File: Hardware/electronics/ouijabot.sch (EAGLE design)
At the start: 12 parts, among them J1 RASPBERRYPI-40-PIN-GPIO_PTH_N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

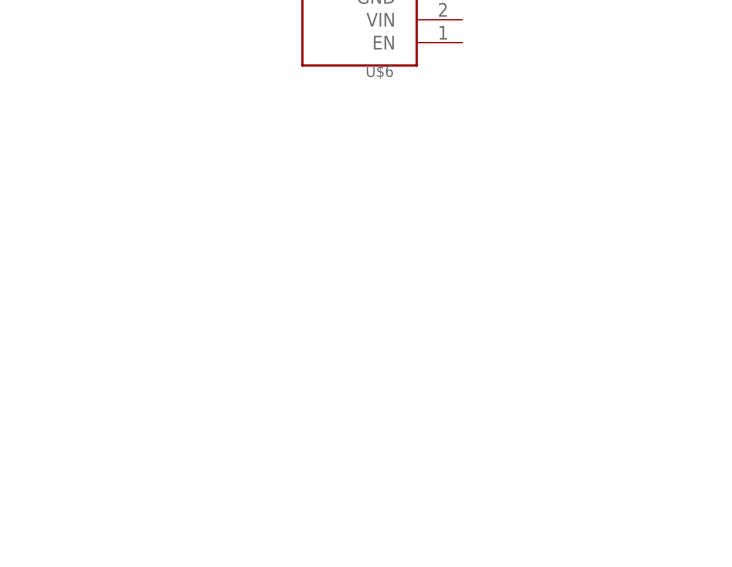
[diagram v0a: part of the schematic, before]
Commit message: Added USB header to schematic.
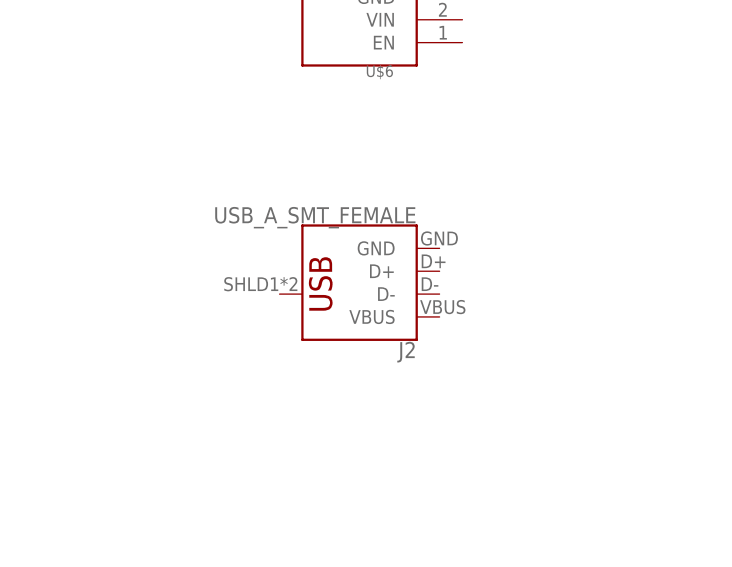
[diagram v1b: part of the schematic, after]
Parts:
- added J2: USB_A_SMT_FEMALE, SparkFun-Connectors:USB_A_SMT_FEMALE
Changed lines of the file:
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@@
 <part name="U$8" library="ouijabot" deviceset="TB9051FTG" device=""/>
 <part name="U$9" library="ouijabot" deviceset="TB9051FTG" device=""/>
+<part name="J2" library="SparkFun-Connectors" deviceset="USB_A" device="_SMT_FEMALE"/>
 </parts>
 <sheets>
@@
 <attribute name="VALUE" x="213.36" y="25.4" size="1.27" layer="96"/>
 </instance>
+<instance part="J2" gate="G$1" x="45.72" y="119.38" smashed="yes" rot="R180">
+<attribute name="NAME" x="50.8" y="111.506" size="1.778" layer="95" font="vector" rot="R180"/>
+<attribute name="VALUE" x="50.8" y="124.714" size="1.778" layer="96" font="vector" rot="R180" align="top-left"/>
+</instance>
 </instances>

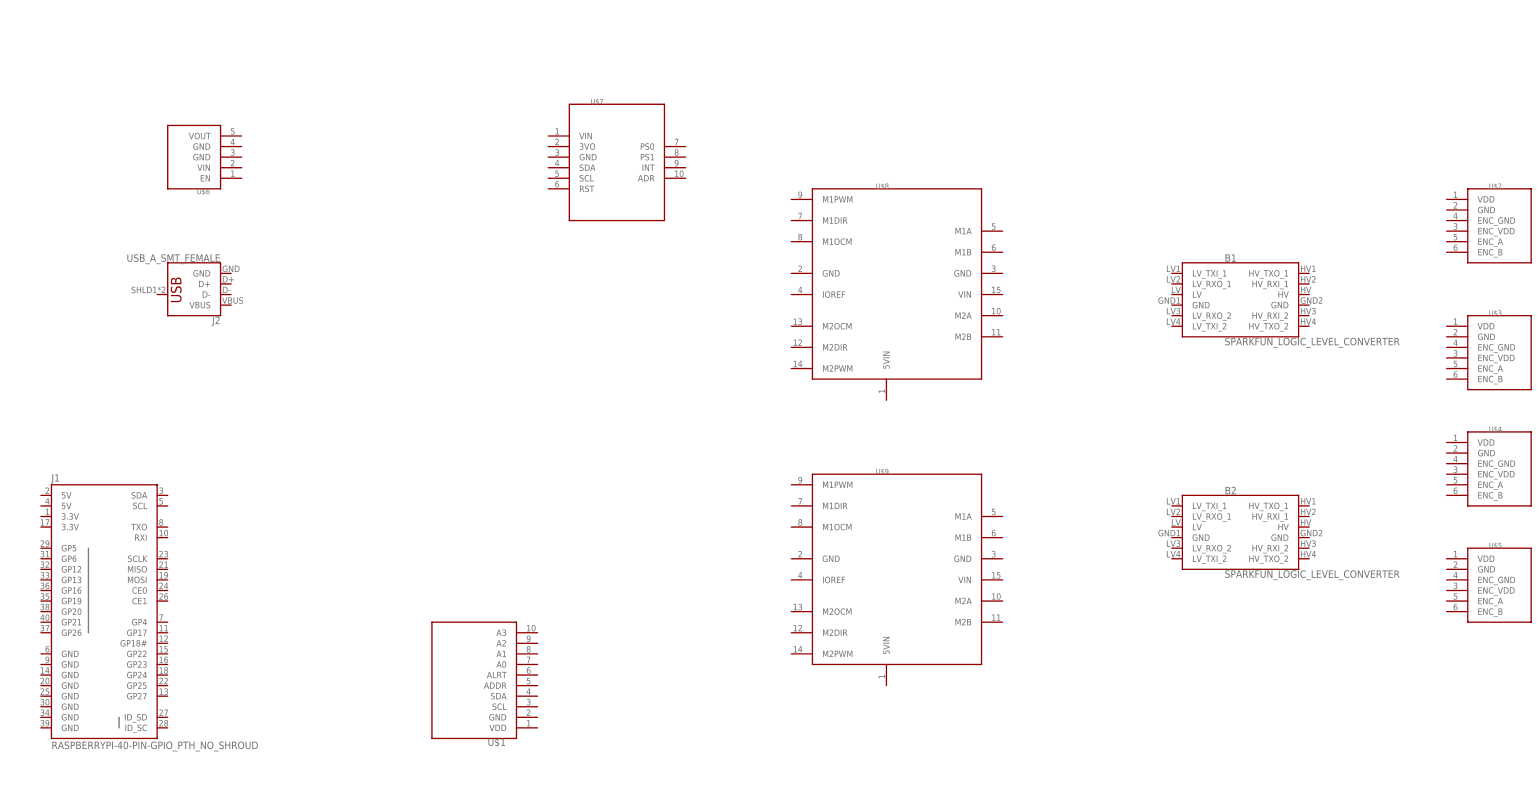
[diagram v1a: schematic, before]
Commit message: First pass of completed schematic.
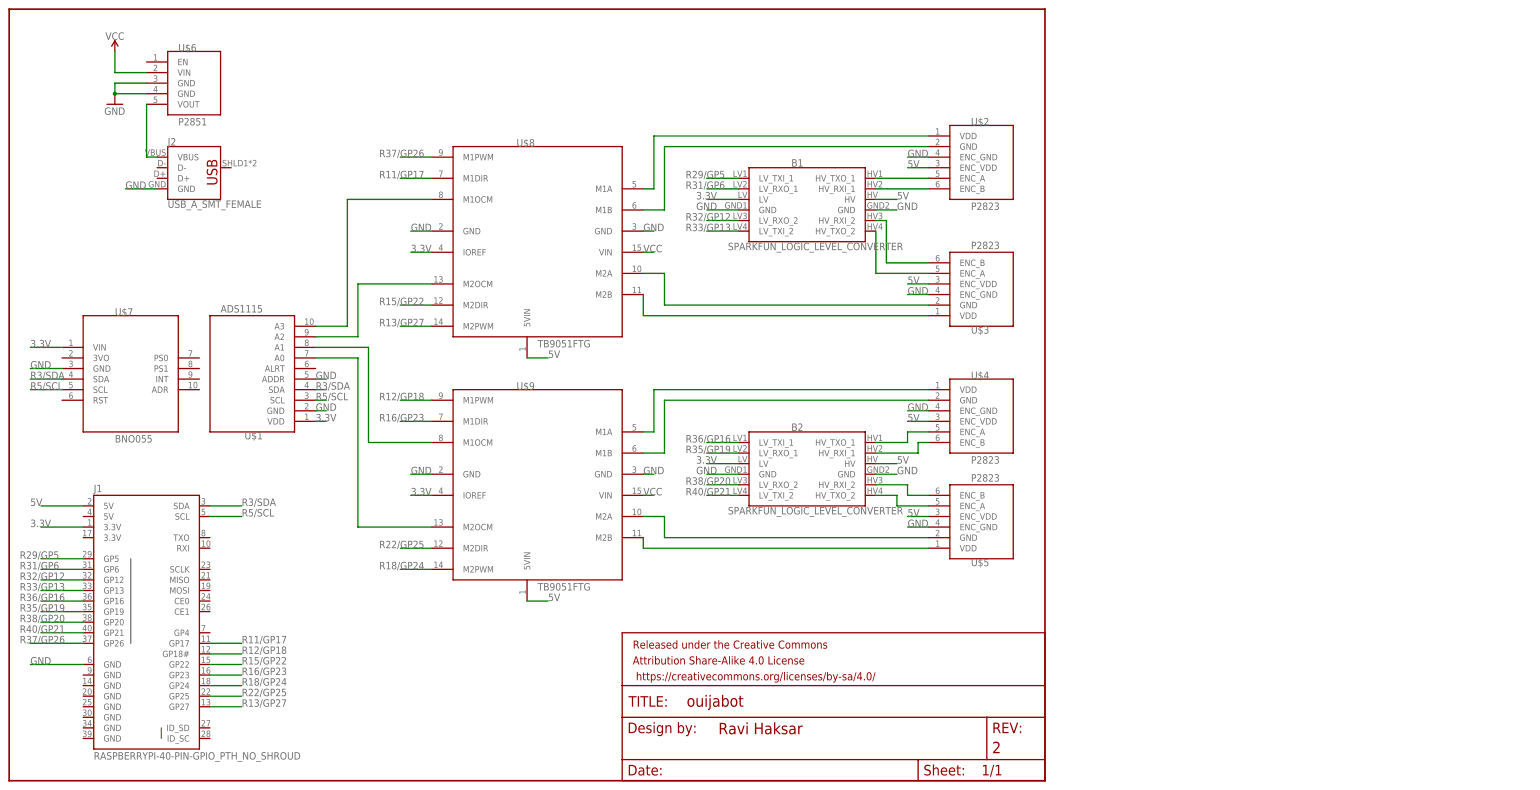
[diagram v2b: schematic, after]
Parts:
- added FRAME1: FRAME-LETTER, SparkFun-Aesthetics:FRAME-LETTER
- U$1: value (none) -> ADS1115
- U$2, U$3, U$4, U$5: value (none) -> P2823
- U$6: value (none) -> P2851
- U$7: value (none) -> BNO055
- U$8, U$9: value (none) -> TB9051FTG
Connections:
- new net 3.3V: B1.LV, B2.LV, J1.3.3V@1, U$1.VDD, U$7.VIN, U$8.IOREF, U$9.IOREF
- new net 5V: B1.HV, B2.HV, J1.5V@2, U$2.ENC_VDD, U$3.ENC_VDD, U$4.ENC_VDD, U$5.ENC_VDD, U$8.5VIN, U$9.5VIN
- new net GND: B1.GND, B1.GND@2, B2.GND, B2.GND@2, J1.GND@6, J2.GND, U$1.ADDR, U$1.GND, U$2.ENC_GND, U$3.ENC_GND, U$4.ENC_GND, U$5.ENC_GND, U$6.GND@1, U$6.GND@2, U$7.GND, U$8.GND@1, U$8.GND@2, U$9.GND@1, U$9.GND@2
- new net N$1: J2.VBUS, U$6.VOUT
- new net N$10: U$4.VDD, U$9.M1A
- new net N$11: U$4.GND, U$9.M1B
- new net N$12: B2.HV_RXI_1, U$4.ENC_B
- new net N$13: B2.HV_TXO_1, U$4.ENC_A
- new net N$14: B2.HV_RXI_2, U$5.ENC_B
- new net N$15: B2.HV_TXO_2, U$5.ENC_A
- new net N$16: U$5.GND, U$9.M2A
- new net N$17: U$5.VDD, U$9.M2B
- new net N$18: U$1.A3, U$8.M1OCM
- new net N$19: U$1.A2, U$8.M2OCM
- new net N$2: U$2.VDD, U$8.M1A
- new net N$20: U$1.A1, U$9.M1OCM
- new net N$21: U$1.A0, U$9.M2OCM
- new net N$3: U$2.GND, U$8.M1B
- new net N$4: B1.HV_TXO_2, U$3.ENC_A
- new net N$5: U$3.GND, U$8.M2A
- new net N$6: B1.HV_TXO_1, U$2.ENC_A
- new net N$7: B1.HV_RXI_1, U$2.ENC_B
- new net N$8: B1.HV_RXI_2, U$3.ENC_B
- new net N$9: U$3.VDD, U$8.M2B
- new net R11/GP17: J1.GP17, U$8.M1DIR
- new net R12/GP18: J1.GP18#, U$9.M1PWM
- new net R13/GP27: J1.GP27, U$8.M2PWM
- new net R15/GP22: J1.GP22, U$8.M2DIR
- new net R16/GP23: J1.GP23, U$9.M1DIR
- new net R18/GP24: J1.GP24, U$9.M2PWM
- new net R22/GP25: J1.GP25, U$9.M2DIR
- new net R29/GP5: B1.LV_TXI_1, J1.GP5
- new net R3/SDA: J1.SDA, U$1.SDA, U$7.SDA
- new net R31/GP6: B1.LV_RXO_1, J1.GP6
- new net R32/GP12: B1.LV_RXO_2, J1.GP12
- new net R33/GP13: B1.LV_TXI_2, J1.GP13
- new net R35/GP19: B2.LV_RXO_1, J1.GP19
- new net R36/GP16: B2.LV_TXI_1, J1.GP16
- new net R37/GP26: J1.GP26, U$8.M1PWM
- new net R38/GP20: B2.LV_RXO_2, J1.GP20
- new net R40/GP21: B2.LV_TXI_2, J1.GP21
- new net R5/SCL: J1.SCL, U$1.SCL, U$7.SCL
- new net VCC: U$6.VIN, U$8.VIN, U$9.VIN
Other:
- moved on the sheet: B1, B2, J1, J2, U$1, U$2, U$3, U$4, U$5, U$6, U$7, U$8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

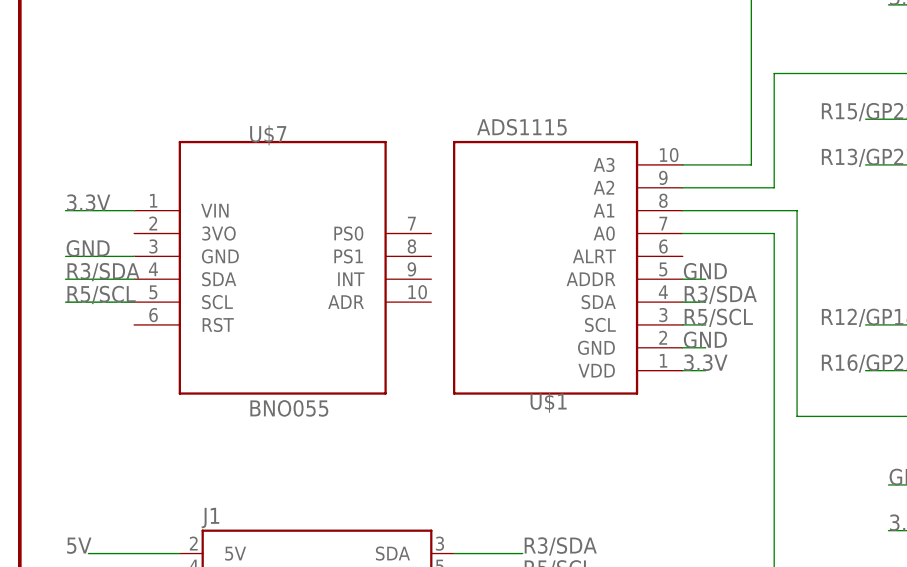
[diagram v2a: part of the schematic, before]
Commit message: Changed IMU and ADC power from 3.3v to 5v due to Raspberry Pi limitations.
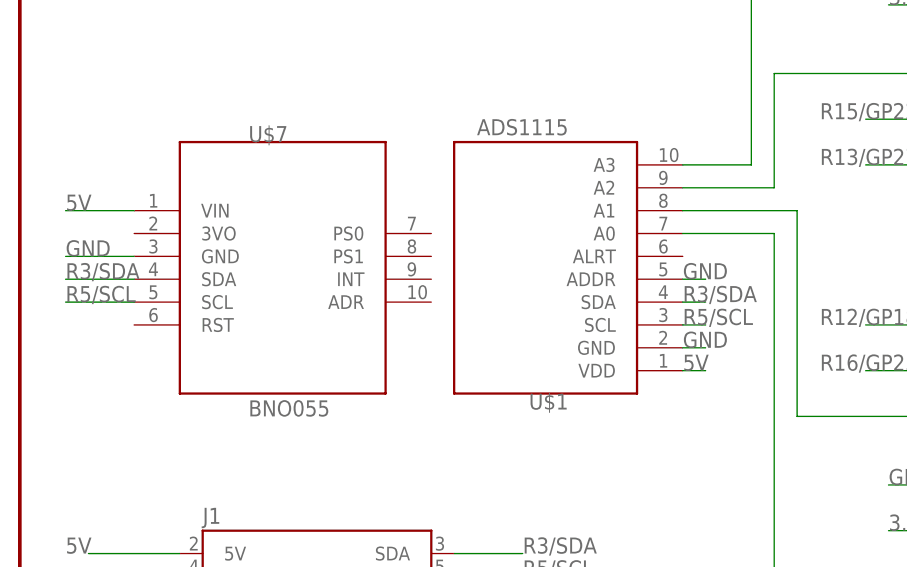
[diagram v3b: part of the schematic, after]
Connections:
- net 3.3V: no longer U$1.VDD, U$7.VIN
- net 5V: now also U$1.VDD, U$7.VIN
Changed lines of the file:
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@@
 <label x="129.54" y="101.6" size="1.778" layer="95"/>
+</segment>
+<segment>
+<pinref part="U$7" gate="G$1" pin="VIN"/>
+<wire x1="12.7" y1="104.14" x2="5.08" y2="104.14" width="0.1524" layer="91"/>
+<label x="5.08" y="104.14" size="1.778" layer="95"/>
+</segment>
+<segment>
+<pinref part="U$1" gate="G$1" pin="VDD"/>
+<wire x1="73.66" y1="86.36" x2="76.2" y2="86.36" width="0.1524" layer="91"/>
+<label x="73.66" y="86.36" size="1.778" layer="95"/>
 </segment>
 </net>
@@
 <label x="96.52" y="68.58" size="1.778" layer="95"/>
 </segment>
-<segment>
-<pinref part="U$1" gate="G$1" pin="VDD"/>
-<wire x1="73.66" y1="86.36" x2="76.2" y2="86.36" width="0.1524" layer="91"/>
-<label x="73.66" y="86.36" size="1.778" layer="95"/>
-</segment>
-<segment>
-<pinref part="U$7" gate="G$1" pin="VIN"/>
-<wire x1="12.7" y1="104.14" x2="5.08" y2="104.14" width="0.1524" layer="91"/>
-<label x="5.08" y="104.14" size="1.778" layer="95"/>
-</segment>
 </net>
